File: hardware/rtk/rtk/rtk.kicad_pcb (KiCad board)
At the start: 2 copper layers, 76.2 x 63.5 mm, 82 parts, among them J1 USB4105-GF-A, J10 Conn_01x02_Pin, J11 Conn_01x06_Pin, J3 B2B-PH-SM4-TBLFSN, J4 Conn_01x02_Pin, J5 Conn_Coaxial, J6 MEM2052-00-195-00-A_REVA, J7 Conn_01x04_Pin, J8 Conn_01x01_Pin, J9 Conn_01x08_Pin, U1 BQ24075RGT, U2 TPS63020DSJR, U3 STM32F765VITx, U4 ZED-F9H-01B, U5 ESP32-S3-ZERO, U6 CORE1262-868M, U7 LSM6DSOX, U8 USB3300-EZK, U9 USBLC6-2SC6, Y1 ASTX-H11-16.000MHZ-T, Y2 ASTX-H11-24.000MHZ-T

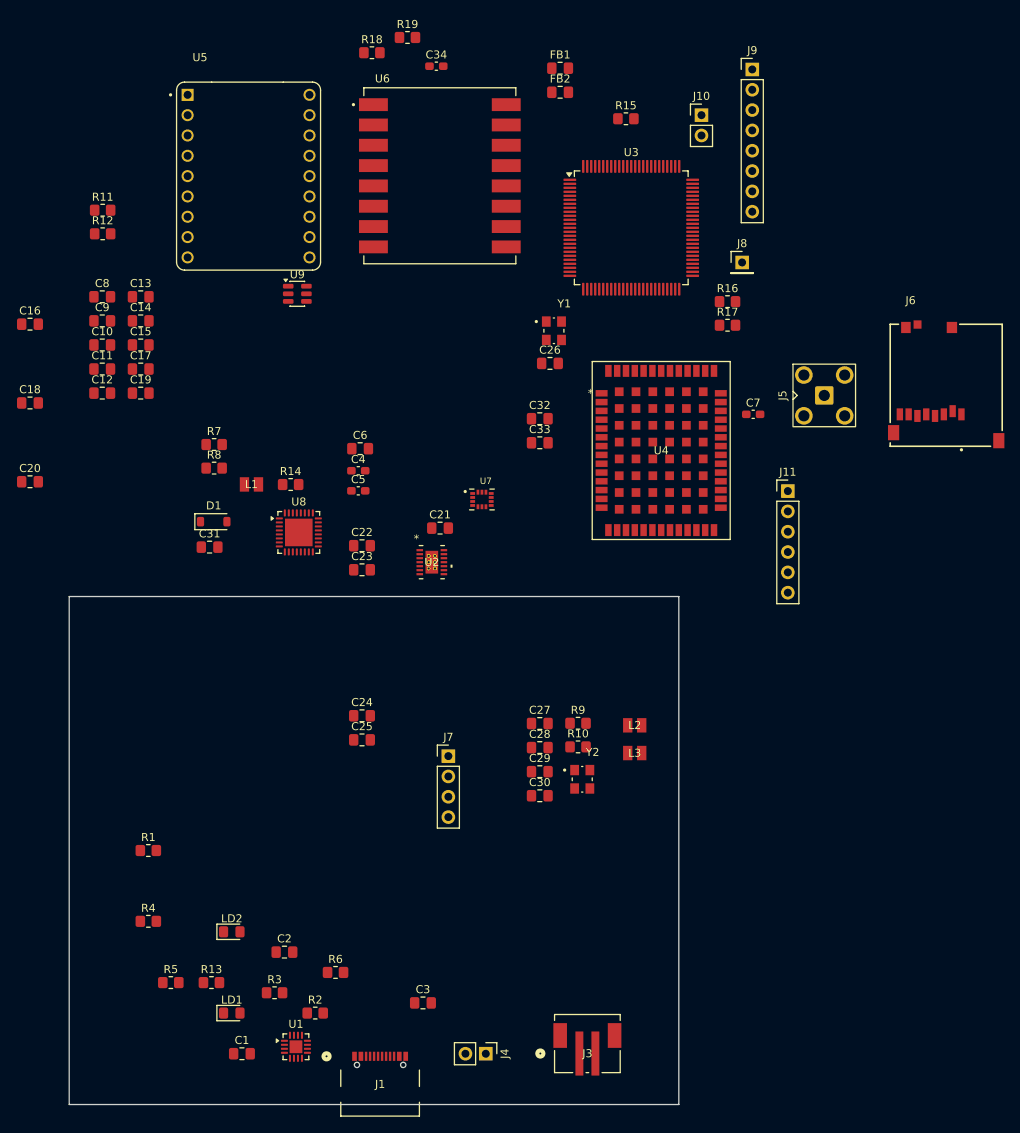
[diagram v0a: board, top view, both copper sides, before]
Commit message: PCB: round 1 initial placement complete
Most components in final positions; some will shift during routing.
Schematic tweaks picked up alongside. Add GCT USB4105 datasheet.

Co-Authored-By: Claude Sonnet 4.6 <noreply@anthropic.com>
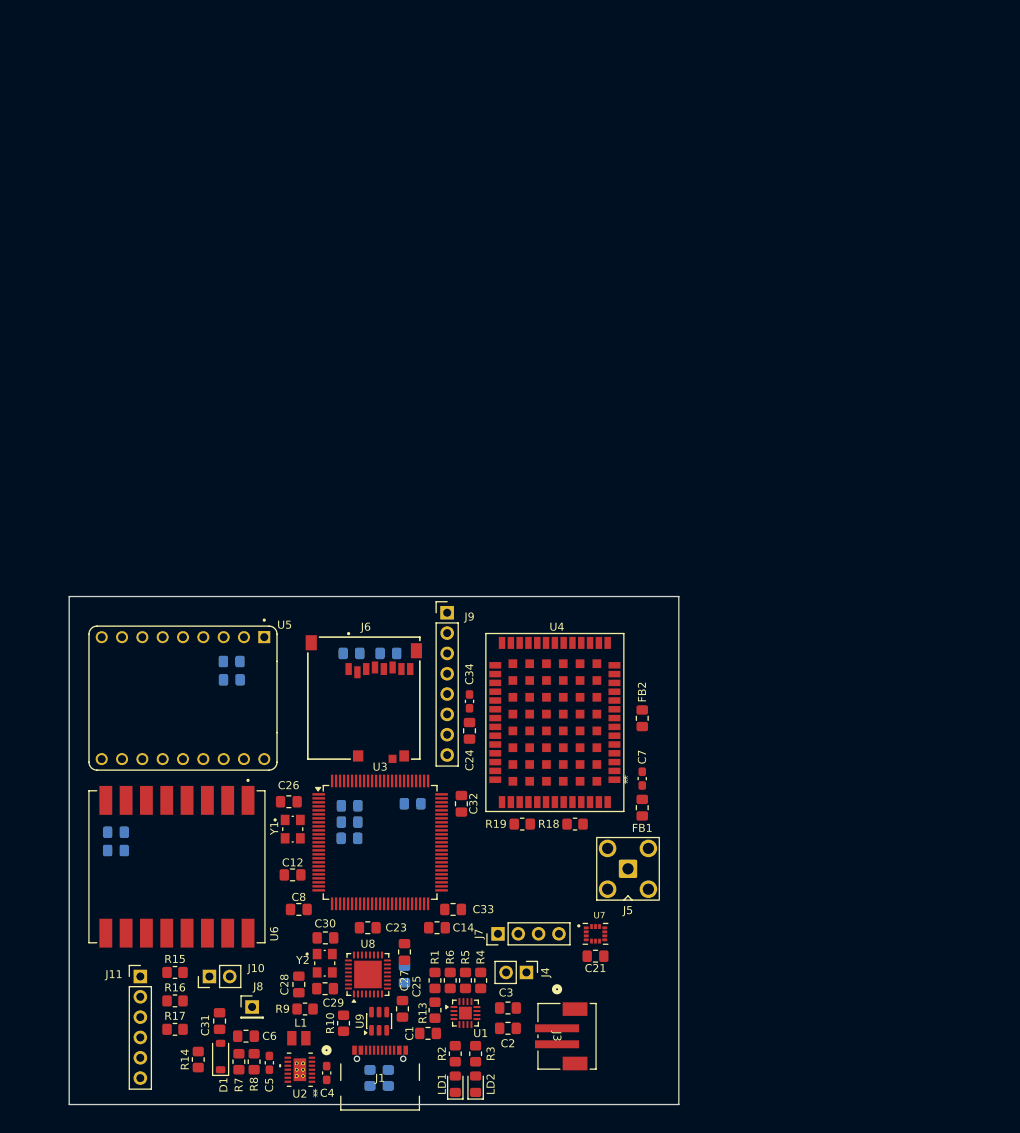
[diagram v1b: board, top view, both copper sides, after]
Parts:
- removed L2, L3: 1uH, DFE201610E-1R0M-P2:IND_DFE2016_2X1P6_MUR
- C10, C11, C13, C15, C16, C17, C18, C19, C20, C22, C9, R11, R12: moved to B.Cu
- C24: value 100n -> 10u
- moved J10 124.0 mm to (119.1, 136.4), turned to 90 degrees
- moved R15 120.7 mm to (114.8, 135.9)
- moved R11 113.5 mm to (139.2, 149.1), turned to -90 degrees
- moved R17 111.9 mm to (114.8, 143.0)
- moved J8 111.4 mm to (124.5, 140.2)
- moved R16 111.4 mm to (114.8, 139.4)
- moved R12 111.4 mm to (141.5, 149.1), turned to -90 degrees
- moved J11 101.2 mm to (110.5, 136.4)
- moved R18 99.7 mm to (164.8, 117.3)
- moved R19 99.4 mm to (158.2, 117.3), turned to 180 degrees
- moved FB1 93.0 mm to (173.2, 115.3), turned to 90 degrees
- moved U6 92.4 mm to (115.1, 122.7), turned to -90 degrees
- moved U9 91.5 mm to (140.3, 142.0), turned to 90 degrees
- moved C14 84.4 mm to (147.6, 130.3)
- moved U3 83.0 mm to (140.5, 119.6)
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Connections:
- C24 pad 1: +3V3 -> GND
- C24 pad 2: GND -> +3V3
- U3 pad 59: I2C4_SCL -> I2C4_SCK
- U7 pad 13: I2C4_SCL -> I2C4_SCK

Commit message: Add LD3/LD4 debug LEDs: schematic, PCB placement, ioc
LD3 green PD5, LD4 red PD6 — open-drain outputs, R20/R21 1k5 pull-ups.
CubeMX regenerated with PD5/PD6 configured. Ready for routing.

Co-Authored-By: Claude Sonnet 4.6 <noreply@anthropic.com>
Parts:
- added LD3: LED, LED_SMD:LED_0805_2012Metric_Pad1.15x1.40mm_HandSolder, F.Cu at (151.9, 120.9)
- added LD4: LED, LED_SMD:LED_0805_2012Metric_Pad1.15x1.40mm_HandSolder, F.Cu at (151.9, 123.2)
- added R20: 1K5, Resistor_SMD:R_0805_2012Metric_Pad1.20x1.40mm_HandSolder, F.Cu at (155.7, 120.9)
- added R21: 1K5, Resistor_SMD:R_0805_2012Metric_Pad1.20x1.40mm_HandSolder, F.Cu at (155.7, 123.2)
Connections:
- U3 pad 86: unconnected-(U3-PD5-Pad86) -> PD5_LD3
- U3 pad 87: unconnected-(U3-PD6-Pad87) -> PD6_LD4

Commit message: Add VBAT monitor: 100k divider to PA1 ADC1_IN1
Two 100k resistors divide VBAT by 2 (VBAT_2) fed to PA1. CubeMX
regenerated with ADC1 IN1 on PA1. HAL ADC driver files added.

Co-Authored-By: Claude Sonnet 4.6 <noreply@anthropic.com>
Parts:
- added R22: 100K, Resistor_SMD:R_0805_2012Metric_Pad1.20x1.40mm_HandSolder, F.Cu at (167.4, 136.9)
- added R23: 100K, Resistor_SMD:R_0805_2012Metric_Pad1.20x1.40mm_HandSolder, F.Cu at (164.3, 135.9)
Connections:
- U3 pad 23: unconnected-(U3-PA1-Pad23) -> VBAT_2

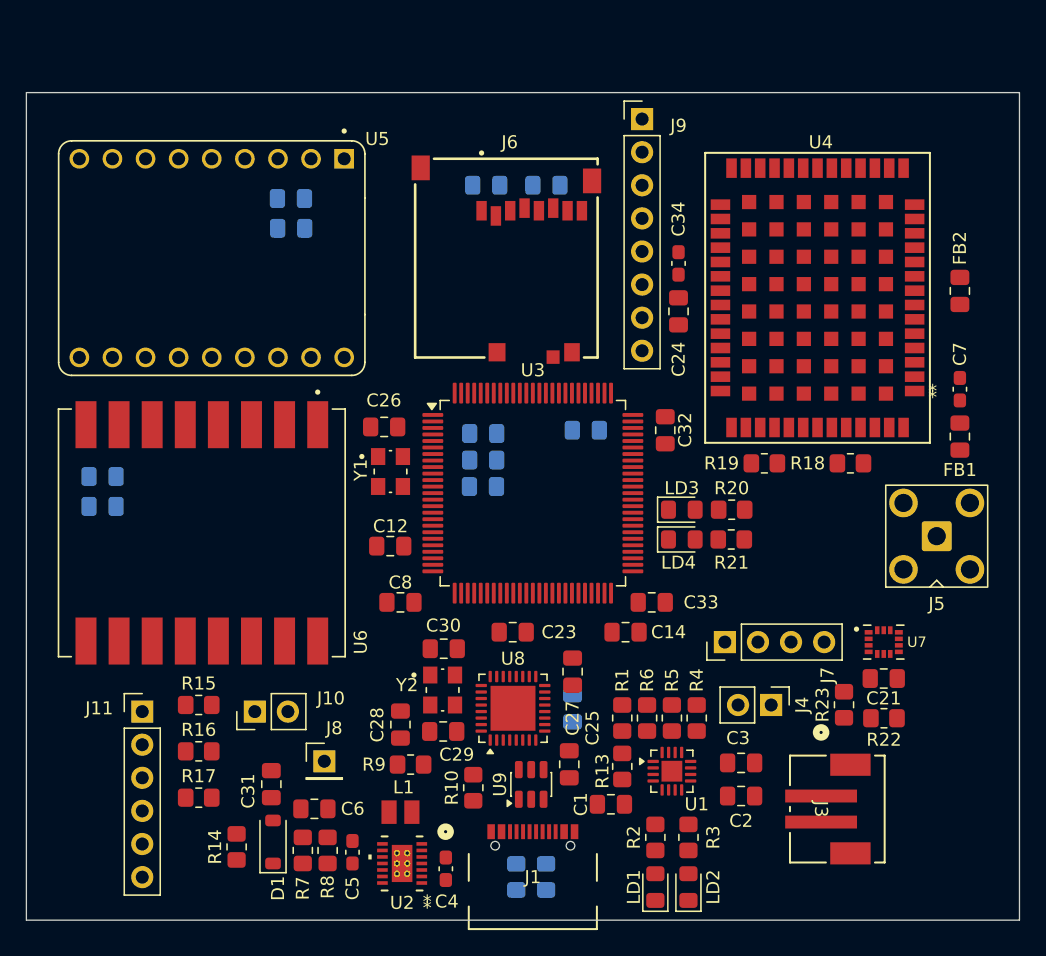
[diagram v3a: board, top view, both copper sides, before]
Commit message: PCB: initial routing complete, pre-DRC snapshot
All signals routed including USB3300 VDD1.8 (pins 15/26 opposite sides,
long perimeter route). Ready for design rules checks.

Co-Authored-By: Claude Sonnet 4.6 <noreply@anthropic.com>
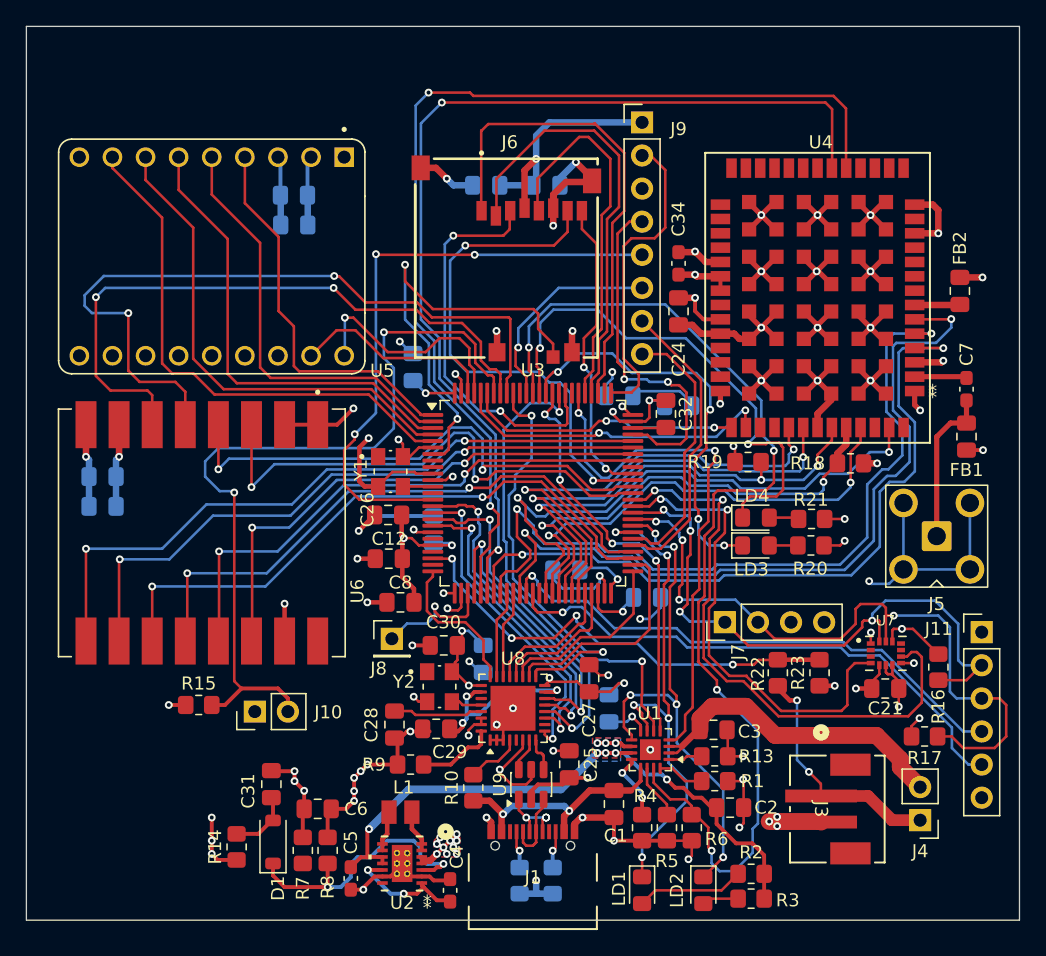
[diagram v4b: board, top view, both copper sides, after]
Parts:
- C14, C23, C33: moved to B.Cu
- moved J11 64.7 mm to (174.9, 130.3)
- moved R16 57.1 mm to (171.6, 133.0), turned to 90 degrees
- moved R17 55.9 mm to (170.5, 138.3), turned to 180 degrees
- moved C14 18.1 mm to (147.1, 112.2), turned to 180 degrees
- moved C10 15.1 mm to (151.6, 112.9), turned to 180 degrees
- moved J4 14.4 mm to (170.2, 144.7), turned to 180 degrees
- moved C11 14.1 mm to (131.3, 110.0), turned to 90 degrees
- moved J8 10.7 mm to (129.6, 130.8)
- moved R4 9.40 mm to (148.8, 145.3), turned to -90 degrees
- moved R6 9.09 mm to (152.7, 145.3), turned to -90 degrees
- moved C13 9.05 mm to (143.0, 125.5), turned to 180 degrees
- moved R22 8.86 mm to (159.3, 133.4), turned to 90 degrees
- moved R1 8.59 mm to (154.4, 141.7), turned to 0 degrees
- moved R5 8.42 mm to (150.7, 145.3), turned to -90 degrees
- moved R2 7.86 mm to (157.2, 148.8), turned to 0 degrees
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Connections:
- net Net-(J4-Pin_2) renamed VBSW
- U2 pad V: (no net) -> GND
- U3 pad 30: unconnected-(U3-PA6-Pad30) -> F9P_GEOFENCE_STAT
- U3 pad 31: unconnected-(U3-PA7-Pad31) -> F9P_RTK_STAT
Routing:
- net GND: track 0.00 -> 283.8 mm, vias 0 -> 70
- net +3V3: track 0.00 -> 139.6 mm, vias 0 -> 45
- net SYSOFF: track 0.00 -> 84.9 mm, vias 0 -> 4
- net F9P_GEOFENCE_STAT: track 0.00 -> 79.2 mm, vias 0 -> 2
- net F9P_RTK_STAT: track 0.00 -> 76.0 mm, vias 0 -> 2
- net BOOT0: track 0.00 -> 62.0 mm, vias 0 -> 2
- net F9P_ANT_OFF: track 0.00 -> 60.4 mm, vias 0 -> 2
- net F9P_ANT_SHORT: track 0.00 -> 60.2 mm, vias 0 -> 2
- net SX1262_SPI2_DIO2: track 0.00 -> 57.1 mm, vias 0 -> 2
- net F9P_ANT_DETECT: track 0.00 -> 57.0 mm, vias 0 -> 2
- net I2C4_SCK: track 0.00 -> 55.2 mm, vias 0 -> 4
- net SX1262_SPI2_BUSY: track 0.00 -> 52.5 mm, vias 0 -> 2
- net +5V: track 0.00 -> 51.9 mm, vias 0 -> 8
- net SX1262_SPI2_DIO1: track 0.00 -> 49.6 mm, vias 0 -> 2
- net SX1262_SPI2_RST: track 0.00 -> 49.2 mm, vias 0 -> 2
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- added copper zone on F.Cu, net +3V3
- added copper zone on In2.Cu, net +3V3
- added copper zone on B.Cu, net +5V
- added copper zone on F.Cu, net +5V
- added copper zone on In1.Cu, net GND
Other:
- board size 76.2 x 63.5 mm -> 76.2 x 68.6 mm
- copper layers 2 -> 4

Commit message: Save routed PCB state before layer annotations and mounting holes
Co-Authored-By: Claude Sonnet 4.6 <noreply@anthropic.com>
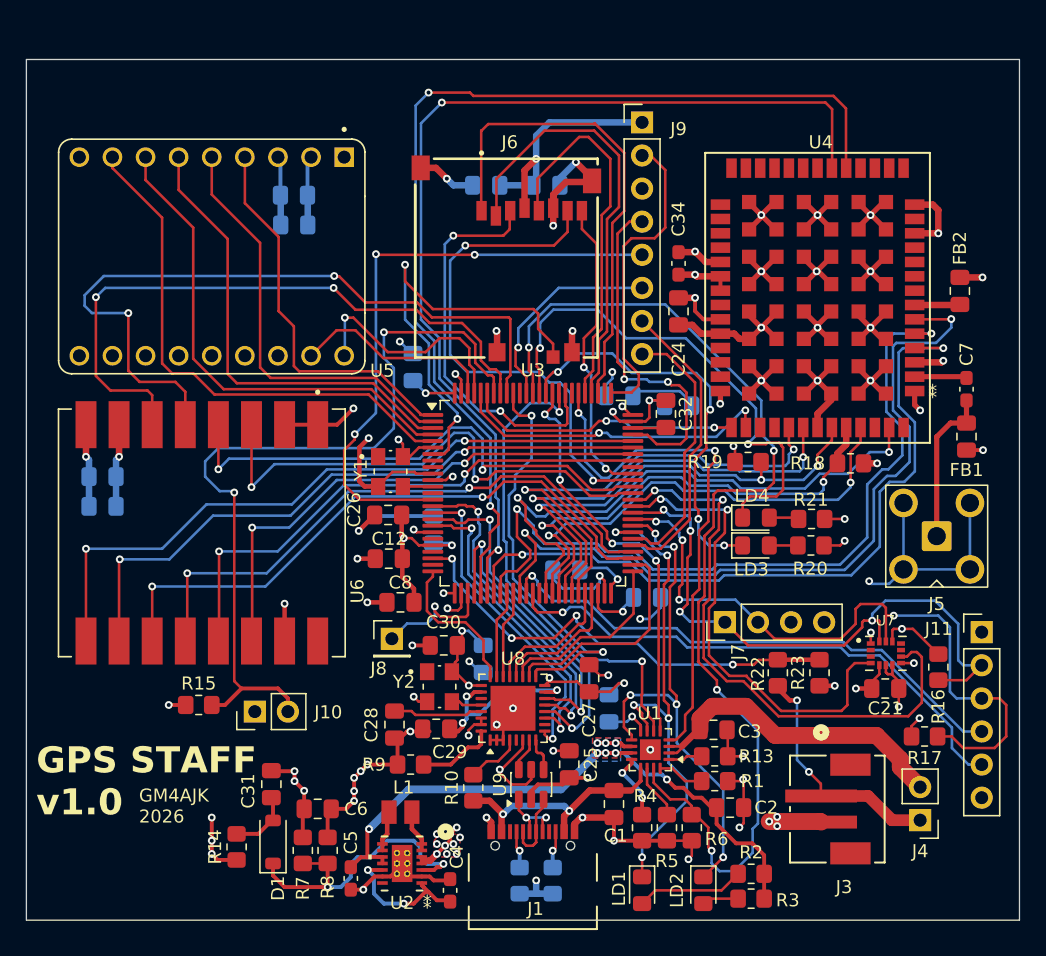
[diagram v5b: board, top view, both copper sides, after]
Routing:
- net SYSOFF: track 84.9 -> 82.5 mm
- net Net-(D1-K): track 21.3 -> 23.2 mm
- net Net-(U2-EN): track 9.32 -> 10.9 mm
- net +3V3: track 139.6 -> 140.1 mm
- net USB_D2_P: vias 3 -> 2
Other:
- board size 76.2 x 68.6 mm -> 76.2 x 66 mm
- board text added: "GM4AJK 2026"
- board text added: "GPS STAFF v1.0"

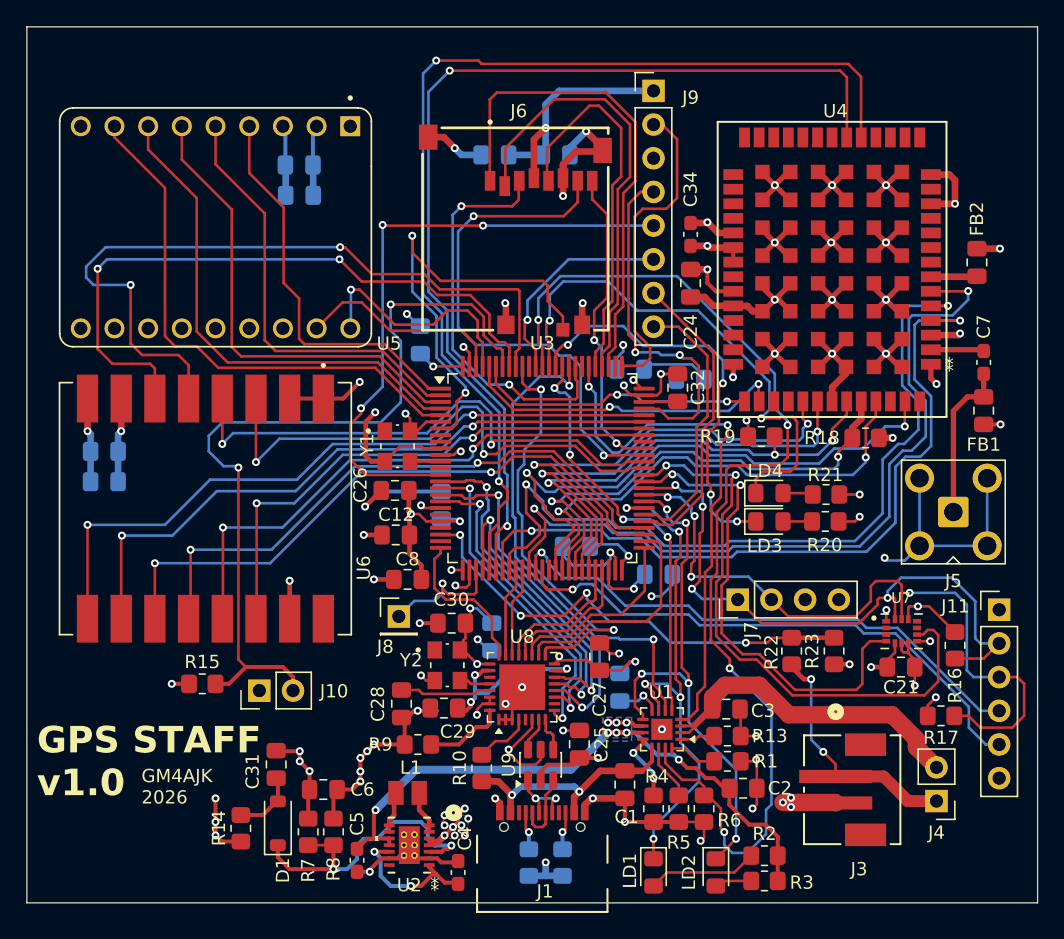
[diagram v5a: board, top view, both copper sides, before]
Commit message: BOM: replace FB2 ferrite bead with L2 bias-T inductor (LQW15AN8N0G8ZD)
Ferrite bead was wrong for the GNSS antenna bias-T RF choke — lossy
resistive impedance absorbs signal. Replaced with Murata 8.0nH wire-wound
inductor (0402). Schematic and PCB updated with new symbol/footprint.

Co-Authored-By: Claude Sonnet 4.6 <noreply@anthropic.com>
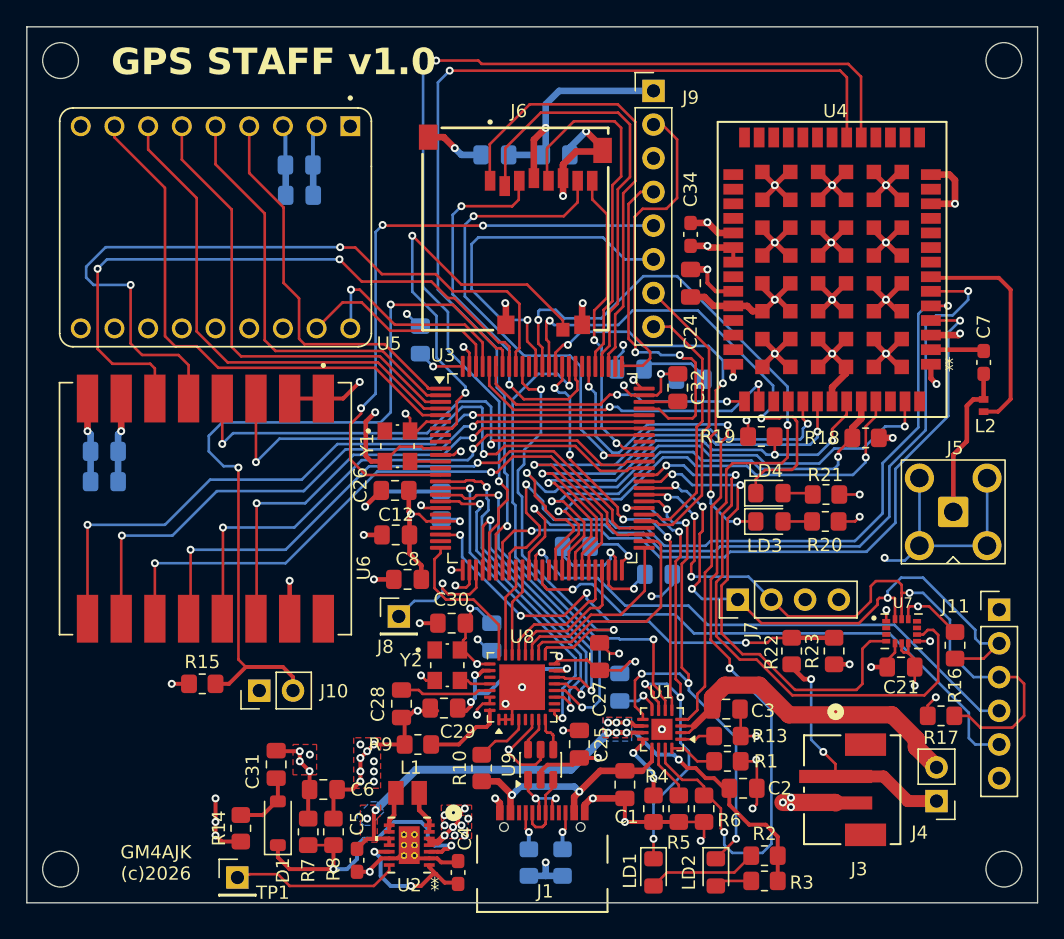
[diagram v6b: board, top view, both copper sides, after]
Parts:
- removed FB1, FB2: FerriteBead_Small, Capacitor_SMD:C_0805_2012Metric_Pad1.18x1.45mm_HandSolder
- added H1: MountingHole, MountingHole:MountingHole_2.7mm, F.Cu at (104.1, 149.9)
- added H2: MountingHole, MountingHole:MountingHole_2.7mm, F.Cu at (175.3, 149.9)
- added H3: MountingHole, MountingHole:MountingHole_2.7mm, F.Cu at (104.1, 88.9)
- added H4: MountingHole, MountingHole:MountingHole_2.7mm, F.Cu at (175.3, 88.9)
- added L2: LQW15AN8N0G8ZD, LQW15AN8N0G8ZD:INDC1006X60N, F.Cu at (173.7, 114.9)
- added TP1: TestPoint, Connector_PinHeader_2.54mm:PinHeader_1x01_P2.54mm_Vertical, F.Cu at (117.5, 150.5)
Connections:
- U2 pad 14: unconnected-(U2-PG-Pad14) -> Net-(U2-PG)
- U2 pad V: GND -> (no net)
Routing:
- net Net-(U4A-VCC_RF): track 3.49 -> 17.1 mm
- net Net-(U2-PG): track 0.00 -> 11.8 mm
- net PB3/SWO: track 16.3 -> 27.0 mm
- net F9P_ANT_DETECT: track 57.0 -> 53.5 mm
- net +3V3: track 140.1 -> 137.1 mm, vias 45 -> 44
- net SDMMC_D2: track 37.6 -> 34.8 mm
- net F9P_ANT_SHORT: track 60.2 -> 57.7 mm
- net PD6_LD4: track 39.6 -> 37.2 mm
- net SDMMC_D0: track 39.8 -> 37.7 mm
- net F9P_ANT_OFF: track 60.4 -> 58.4 mm
- net I2C4_SDA: track 48.4 -> 46.6 mm
- net ESP32_TX: track 18.0 -> 16.3 mm
- net SDMMC_CD: track 33.8 -> 32.2 mm
- net I2C4_SCK: track 55.2 -> 53.6 mm
- net BOOT0: track 62.0 -> 60.5 mm
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- added copper zone on F.Cu, net GND
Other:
- board text added: "GM4AJK (c)2026"
- board text added: "Mtg Hole 2.5mm"
- board text removed: "GM4AJK 2026"
